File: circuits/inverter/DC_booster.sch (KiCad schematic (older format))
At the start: 0 parts

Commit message: Add more circuitry, add library content
AC current measurement
AC filter
AC switch
DC booster
DC input
Analog frontend
drivers
inverter
main controller
power supply

new components for:
standard library (e.g. relay)
AC current sensor acs722
voltage regulator LM317L

Footprints for:
AC relay
TO-220
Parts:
- added C?: 1µ/25V, symbol Capacitor
- added C? (x3): 220p, symbol Capacitor
- added C?: 330p, symbol Capacitor
- added C? (x2): 3n3/600V, symbol Capacitor
- added C? (x3): Capacitor_pol, symbol Capacitor_pol
- added D? (x2): BAT54, symbol Schottky
- added D?: Diode, symbol Diode
- added L?: Inductor, symbol Inductor
- added Q? (x3): BSS138, symbol NMOS
- added Q? (x2): BSS84, symbol PMOS
- added Q?: IGBT, symbol IGBT
- added R? (x2): 2k0, symbol Resistor
- added R?: 10k, symbol Resistor
- added R?: 1k0, symbol Resistor
- added R?: 4k7, symbol Resistor
- added R?: 10, symbol Resistor
- added R?: 4k2, symbol Resistor
- added R?: 1k2, symbol Resistor
- added R? (x3): 22, OSSI_standard_footprints:MELF_0204_W, symbol Resistor
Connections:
- net labels added: +15V, +3V3, Boost_T1i, DC+, DC_link+, GND
- wire segments 0 -> 69

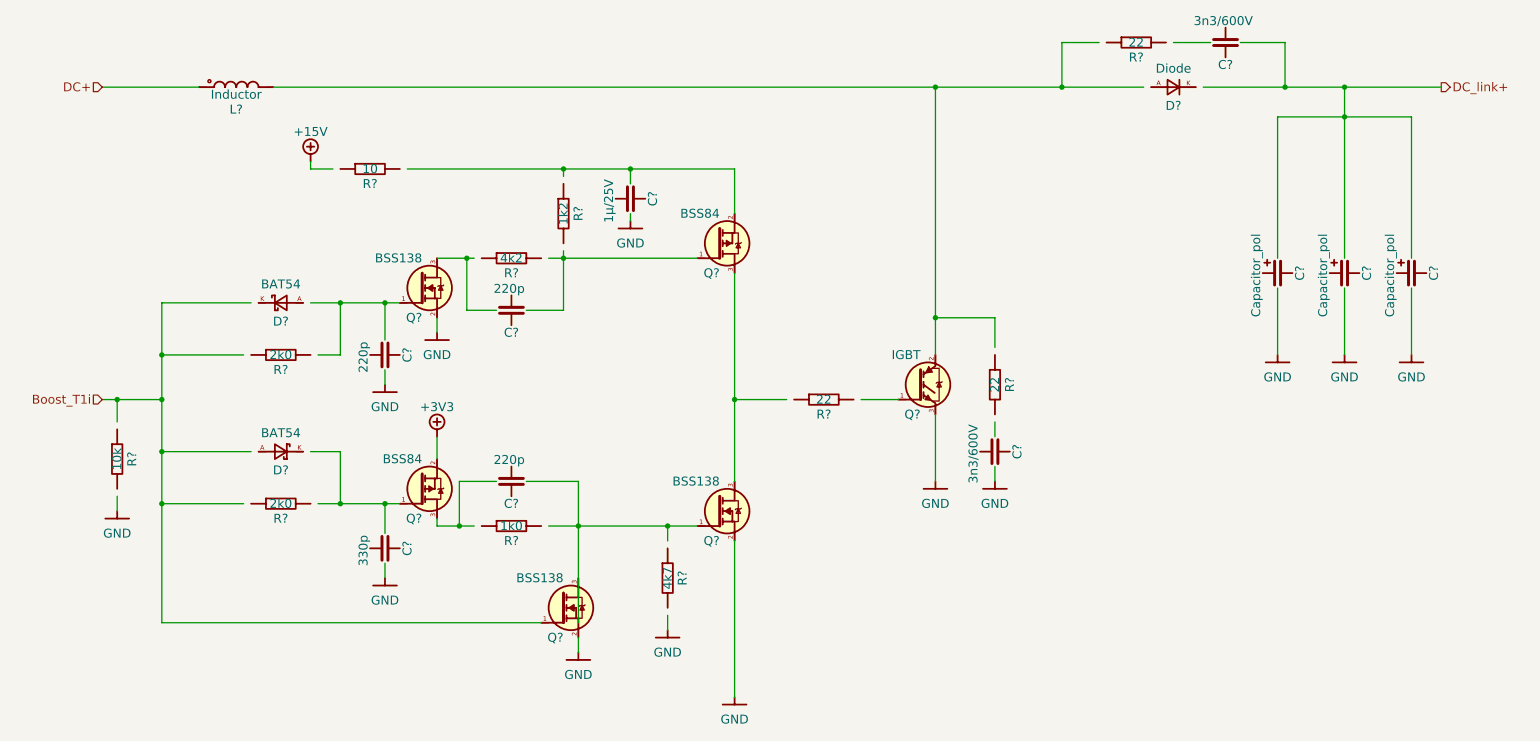
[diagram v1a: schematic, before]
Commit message: Updates all schematic pages to current components
all components are replaced with the current component library parts
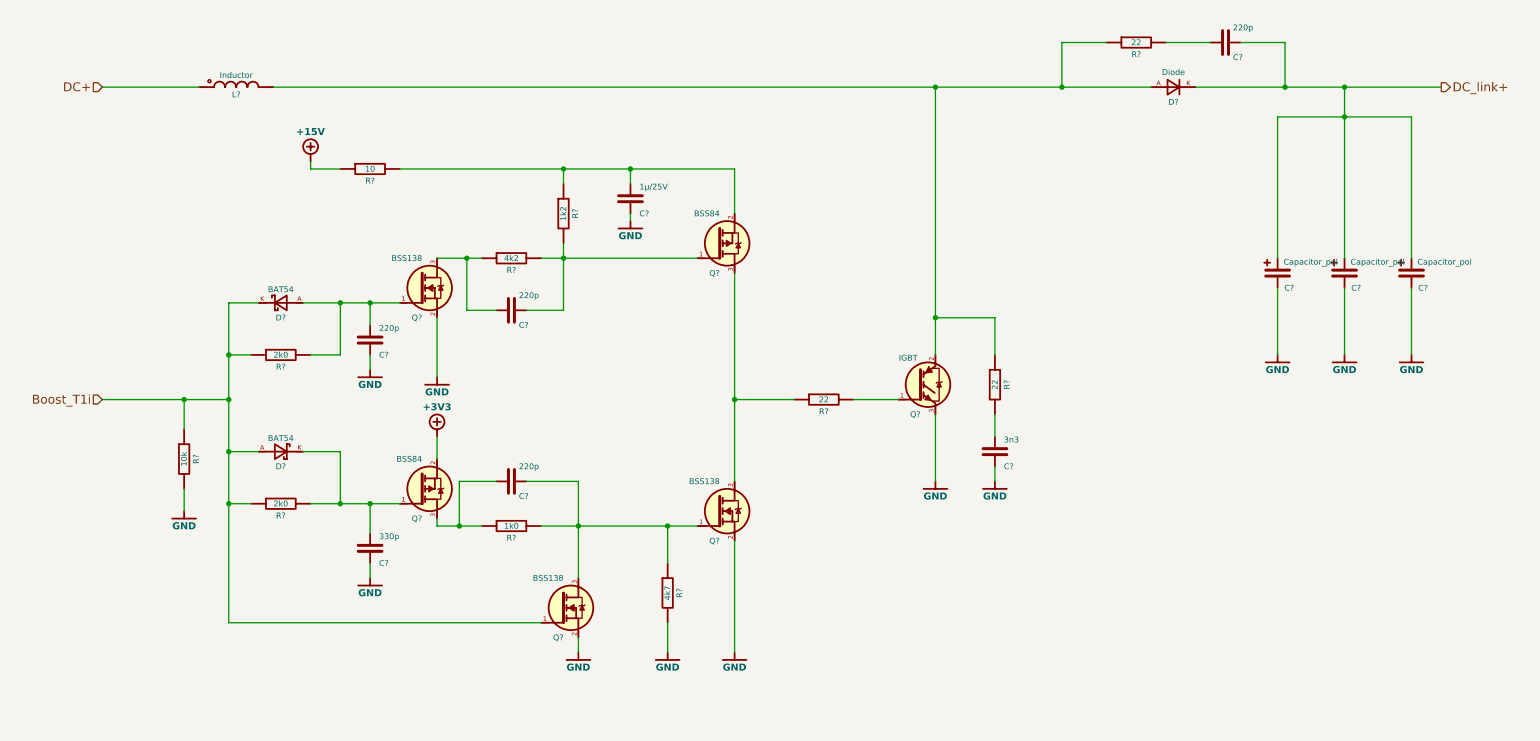
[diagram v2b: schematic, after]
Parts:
- removed C?: 1µ/25V, symbol Capacitor
- removed C? (x3): 220p, symbol Capacitor
- removed C?: 330p, symbol Capacitor
- removed C? (x2): 3n3/600V, symbol Capacitor
- removed C? (x3): Capacitor_pol, symbol Capacitor_pol
- removed D? (x2): BAT54, symbol Schottky
- removed D?: Diode, symbol Diode
- removed L?: Inductor, symbol Inductor
- removed Q? (x3): BSS138, symbol NMOS
- removed Q? (x2): BSS84, symbol PMOS
- removed Q?: IGBT, symbol IGBT
- removed R? (x2): 2k0, symbol Resistor
- removed R?: 10k, symbol Resistor
- removed R?: 1k0, symbol Resistor
- removed R?: 4k7, symbol Resistor
- removed R?: 10, symbol Resistor
- removed R?: 4k2, symbol Resistor
- removed R?: 1k2, symbol Resistor
- removed R? (x3): 22, OSSI_standard_footprints:MELF_0204_W, symbol Resistor
- added C?: 1µ/25V, symbol Capacitor
- added C? (x4): 220p, symbol Capacitor
- added C?: 330p, symbol Capacitor
- added C?: 3n3, symbol Capacitor
- added C? (x3): Capacitor_pol, symbol Capacitor_pol
- added D? (x2): BAT54, symbol Schottky
- added D?: Diode, symbol Diode
- added L?: Inductor, symbol Inductor
- added Q? (x2): BSS84, symbol PMOS
- added Q? (x3): BSS138, symbol NMOS
- added Q?: IGBT, symbol IGBT
- added R?: 10, symbol Resistor
- added R?: 4k2, symbol Resistor
- added R?: 1k2, symbol Resistor
- added R? (x2): 2k0, symbol Resistor
- added R?: 1k0, symbol Resistor
- added R?: 4k7, symbol Resistor
- added R? (x3): 22, symbol Resistor
- added R?: 10k, symbol Resistor
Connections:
- wire segments 69 -> 95

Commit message: bulk-updates libraries and schematics
schematic is updated to Kicad 5.1.14
updates various sheets with new circuits
adds various component libraries
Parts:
- removed L?: Inductor, symbol Inductor
- added L?: Inductor, symbol OSSI_standard_components:Inductor
- C? (x7): symbol Capacitor -> OSSI_standard_components:Capacitor
- C? (x3): symbol Capacitor_pol -> OSSI_standard_components:Capacitor_pol
- D? (x2): symbol Schottky -> OSSI_standard_components:Schottky
- D?: symbol Diode -> OSSI_standard_components:Diode
- Q? (x2): symbol PMOS -> OSSI_standard_components:PMOS
- Q? (x3): symbol NMOS -> OSSI_standard_components:NMOS
- Q?: symbol IGBT -> OSSI_standard_components:IGBT
- R? (x11): symbol Resistor -> OSSI_standard_components:Resistor
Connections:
- net DC+: now also L?.1
- net at D?.A, Q?.2 (C), R?.1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: now also L?.2
- net +15V: now reaches R?.1
- net GND: now reaches C?.1
- net GND: now also C?.-, C?.-, C?.-, C?.1, C?.1, C?.1, Q?.2 (S), Q?.2 (S), Q?.2 (S), Q?.3 (E), R?.2, R?.2
- net +3V3: now reaches Q?.2 (S)
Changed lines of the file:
@@
-EESchema Schematic File Version 2
-LIBS:lm317
-LIBS:kv30f
-LIBS:OSSI_standard_components
-LIBS:connectors
-LIBS:lm4030
-LIBS:acs722
+EESchema Schematic File Version 4
 LIBS:OSSI_MK_I-cache
-EELAYER 25 0
+EELAYER 30 0
 EELAYER END
 $Descr A4 11693 8268
@@
 Boost_T1i
 $Comp
-L Inductor L?
-U 1 1 58D7F810
-P 2200 1050
-F 0 "L?" H 2200 1000 39  0000 C CNN
-F 1 "Inductor" H 2200 1130 39  0000 C CNN
-F 2 "" H 2200 1205 35  0000 C CNN
-F 3 "" H 2200 1050 60  0000 C CNN
-F 4 "M" H 2370 1235 35  0001 L CNN "Manufacturer"
-F 5 "P" H 2370 1180 35  0001 L CNN "Partnumber"
-F 6 "S" H 2370 1290 35  0001 L CNN "Supplier"
-F 7 "O.No." H 2370 1340 35  0001 L CNN "Order No."
-	1    2200 1050
-	1    0    0    -1
-$EndComp
-$Comp
-L Resistor R?
+L OSSI_standard_components:Resistor R?
 U 1 1 58D7F88F
 P 3100 1600
@@
 $EndComp
 $Comp
-L Resistor R?
+L OSSI_standard_components:Resistor R?
 U 1 1 58D7FFA2
 P 4050 2200
@@
 $EndComp
 $Comp
-L Resistor R?
+L OSSI_standard_components:Resistor R?
 U 1 1 58D800DB
 P 4400 1900
@@
 $EndComp
 $Comp
-L Capacitor C?
+L OSSI_standard_components:Capacitor C?
 U 1 1 58D80A4E
 P 4850 1800
@@
 $EndComp
 $Comp
-L PMOS Q?
+L OSSI_standard_components:PMOS Q?
 U 1 1 58D80C47
 P 5450 2100
@@
 $EndComp
 $Comp
-L Capacitor C?
+L OSSI_standard_components:Capacitor C?
 U 1 1 58D8166D
 P 4050 2550
@@
 $EndComp
 $Comp
-L NMOS Q?
+L OSSI_standard_components:NMOS Q?
 U 1 1 58D81E73
 P 3450 2400
@@
 $EndComp
 $Comp
-L Capacitor C?
+L OSSI_standard_components:Capacitor C?
 U 1 1 58D8231E
 P 3100 2750
@@
 $EndComp
 $Comp
-L GND #GND015
+L OSSI_standard_components:GND #GND?
 U 1 1 58D824A2
 P 4850 1950
-F 0 "#GND015" H 4850 1760 60  0001 C CNN
+F 0 "#GND?" H 4850 1760 60  0001 C CNN
 F 1 "GND" H 4850 1850 47  0000 C CNB
 F 2 "" H 4850 1950 60  0000 C CNN
@@
 $EndComp
 $Comp
-L GND #GND016
+L OSSI_standard_components:GND #GND?
 U 1 1 58D82616
 P 3550 3000
-F 0 "#GND016" H 3550 2810 60  0001 C CNN
+F 0 "#GND?" H 3550 2810 60  0001 C CNN
 F 1 "GND" H 3550 2900 47  0000 C CNB
 F 2 "" H 3550 3000 60  0000 C CNN
@@
 $EndComp
 $Comp
-L GND #GND017
+L OSSI_standard_components:GND #GND?
 U 1 1 58D8267E
 P 3100 2950
-F 0 "#GND017" H 3100 2760 60  0001 C CNN
+F 0 "#GND?" H 3100 2760 60  0001 C CNN
 F 1 "GND" H 3100 2850 47  0000 C CNB
 F 2 "" H 3100 2950 60  0000 C CNN
@@
 $EndComp
 $Comp
-L Resistor R?
+L OSSI_standard_components:Resistor R?
 U 1 1 58D828FA
 P 2500 2850
@@
 $EndComp
 $Comp
-L Schottky D?
+L OSSI_standard_components:Schottky D?
 U 1 1 58D82B05
 P 2500 2500
@@
 $EndComp
 $Comp
-L Schottky D?
+L OSSI_standard_components:Schottky D?
 U 1 1 58D83271
 P 2500 3500
@@
 $EndComp
 $Comp
-L Resistor R?
+L OSSI_standard_components:Resistor R?
 U 1 1 58D8330E
 P 2500 3850
@@
 $EndComp
 Wire Wire Line
-	1300 1050 1950 1050
-Wire Wire Line
-	2450 1050 6900 1050
+	1300 1050 5125 1050
+Wire Wire Line
+	5625 1050 6900 1050
 Wire Wire Line
 	6900 1050 7750 1050
@@
 	10100 2400 10100 2850
 $Comp
-L Capacitor C?
+L OSSI_standard_components:Capacitor C?
 U 1 1 58D83762
 P 3100 4150
@@
 $EndComp
 $Comp
-L PMOS Q?
+L OSSI_standard_components:PMOS Q?
 U 1 1 58D83933
 P 3450 3750
@@
 $EndComp
 $Comp
-L Capacitor C?
+L OSSI_standard_components:Capacitor C?
 U 1 1 58D83A53
 P 4050 3700
@@
 $EndComp
 $Comp
-L Resistor R?
+L OSSI_standard_components:Resistor R?
 U 1 1 58D83B16
 P 4050 4000
@@
 $EndComp
 $Comp
-L NMOS Q?
+L OSSI_standard_components:NMOS Q?
 U 1 1 58D84080
 P 4400 4550
@@
 $EndComp
 $Comp
-L Resistor R?
+L OSSI_standard_components:Resistor R?
 U 1 1 58D84385
 P 5100 4450
@@
 $EndComp
 $Comp
-L NMOS Q?
+L OSSI_standard_components:NMOS Q?
 U 1 1 58D84654
 P 5450 3900
@@
 $EndComp
 $Comp
-L Resistor R?
+L OSSI_standard_components:Resistor R?
 U 1 1 58D84A1F
 P 6150 3150
@@
 $EndComp
 $Comp
-L Capacitor C?
+L OSSI_standard_components:Capacitor C?
 U 1 1 58D84FBF
 P 7300 3500
@@
 $EndComp
 $Comp
-L Resistor R?
+L OSSI_standard_components:Resistor R?
 U 1 1 58D852FD
 P 7300 3050
@@
 $EndComp
 $Comp
-L IGBT Q?
+L OSSI_standard_components:IGBT Q?
 U 1 1 58D85492
 P 6800 3050
@@
 $EndComp
 $Comp
-L Diode D?
+L OSSI_standard_components:Diode D?
 U 1 1 58D858BF
 P 8500 1050
@@
 $EndComp
 $Comp
-L Resistor R?
+L OSSI_standard_components:Resistor R?
 U 1 1 58D85C8D
 P 8250 750
@@
 $EndComp
 $Comp
-L Capacitor C?
+L OSSI_standard_components:Capacitor C?
 U 1 1 58D8665C
 P 8850 750
@@
 $EndComp
 $Comp
-L Capacitor_pol C?
+L OSSI_standard_components:Capacitor_pol C?
 U 1 1 58D86DDF
 P 9200 2300
@@
 $EndComp
 $Comp
-L Capacitor_pol C?
+L OSSI_standard_components:Capacitor_pol C?
 U 1 1 58D873CF
 P 9650 2300
@@
 $EndComp
 $Comp
-L Capacitor_pol C?
+L OSSI_standard_components:Capacitor_pol C?
 U 1 1 58D8744F
 P 10100 2300
@@
 $EndComp
 $Comp
-L Resistor R?
+L OSSI_standard_components:Resistor R?
 U 1 1 58D87C36
 P 1850 3550
@@
 $EndComp
 $Comp
-L GND #GND?
+L OSSI_standard_components:GND #GND?
 U 1 1 58E1EA26
 P 1850 3900
@@
 $EndComp
 $Comp
-L GND #GND?
+L OSSI_standard_components:GND #GND?
 U 1 1 58E1EA8E
 P 3100 4350
@@
 $EndComp
 $Comp
-L GND #GND?
+L OSSI_standard_components:GND #GND?
 U 1 1 58E1EAF6
 P 4500 4850
@@
 $EndComp
 $Comp
-L GND #GND?
+L OSSI_standard_components:GND #GND?
 U 1 1 58E1EB5E
 P 5100 4850
@@
 $EndComp
 $Comp
-L GND #GND?
+L OSSI_standard_components:GND #GND?
 U 1 1 58E1EBC6
 P 5550 4850
@@
 $EndComp
 $Comp
-L GND #GND?
+L OSSI_standard_components:GND #GND?
 U 1 1 58E1EC2E
 P 6900 3700
@@
 $EndComp
 $Comp
-L GND #GND?
+L OSSI_standard_components:GND #GND?
 U 1 1 58E1EC96
 P 7300 3700
@@
 $EndComp
 $Comp
-L GND #GND?
+L OSSI_standard_components:GND #GND?
 U 1 1 58E1ECFE
 P 9200 2850
@@
 $EndComp
 $Comp
-L GND #GND?
+L OSSI_standard_components:GND #GND?
 U 1 1 58E1ED66
 P 9650 2850
@@
 $EndComp
 $Comp
-L GND #GND?
+L OSSI_standard_components:GND #GND?
 U 1 1 58E1EDCE
 P 10100 2850
@@
 $EndComp
 $Comp
-L +15V #+15V?
+L OSSI_standard_components:+15V #+15V?
 U 1 1 58E3805F
 P 2700 1550
@@
 $EndComp
 $Comp
-L +3V3 #+3V3?
+L OSSI_standard_components:+3V3 #+3V?
 U 1 1 58E381A9
 P 3550 3400
-F 0 "#+3V3?" H 3550 3675 60  0001 C CNN
+F 0 "#+3V?" H 3550 3675 60  0001 C CNN
 F 1 "+3V3" H 3550 3600 47  0000 C CNB
 F 2 "" H 3550 3400 60  0000 C CNN
@@
 	1    0    0    -1
 $EndComp
+$Comp
+L OSSI_standard_components:Inductor L?
+U 1 1 5CD7F9AC
+P 5375 1050
+F 0 "L?" H 5375 1000 39  0000 C CNN
+F 1 "Inductor" H 5375 1130 39  0000 C CNN
+F 2 "" H 5375 1205 35  0000 C CNN
+F 3 "" H 5375 1050 60  0000 C CNN
+F 4 "M" H 5545 1235 35  0001 L CNN "Manufacturer"
+F 5 "P" H 5545 1180 35  0001 L CNN "Partnumber"
+F 6 "S" H 5545 1290 35  0001 L CNN "Supplier"
+F 7 "O.No." H 5545 1340 35  0001 L CNN "Order No."
+	1    5375 1050
+	1    0    0    -1
+$EndComp
